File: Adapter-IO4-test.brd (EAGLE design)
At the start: 50 x 50 mm, 19 parts, among them CON1 RJ12/6, CON2 0.100, Q1 P-FET, Q2 P-FET, Q3 P-FET, Q4 P-FET, SW1 SPST-MOM, SW2 SPST-MOM, SW3 SPST-MOM, SW4 SPST-MOM

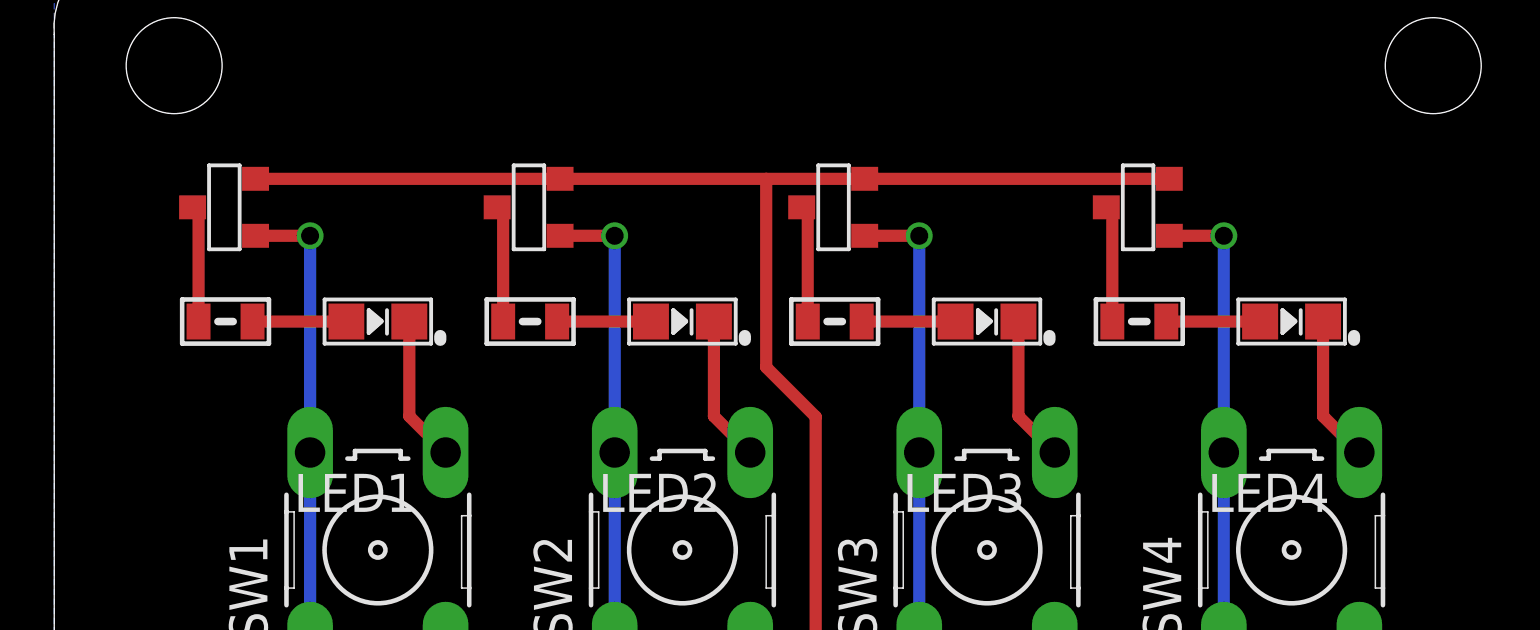
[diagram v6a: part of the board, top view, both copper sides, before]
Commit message: normalized values
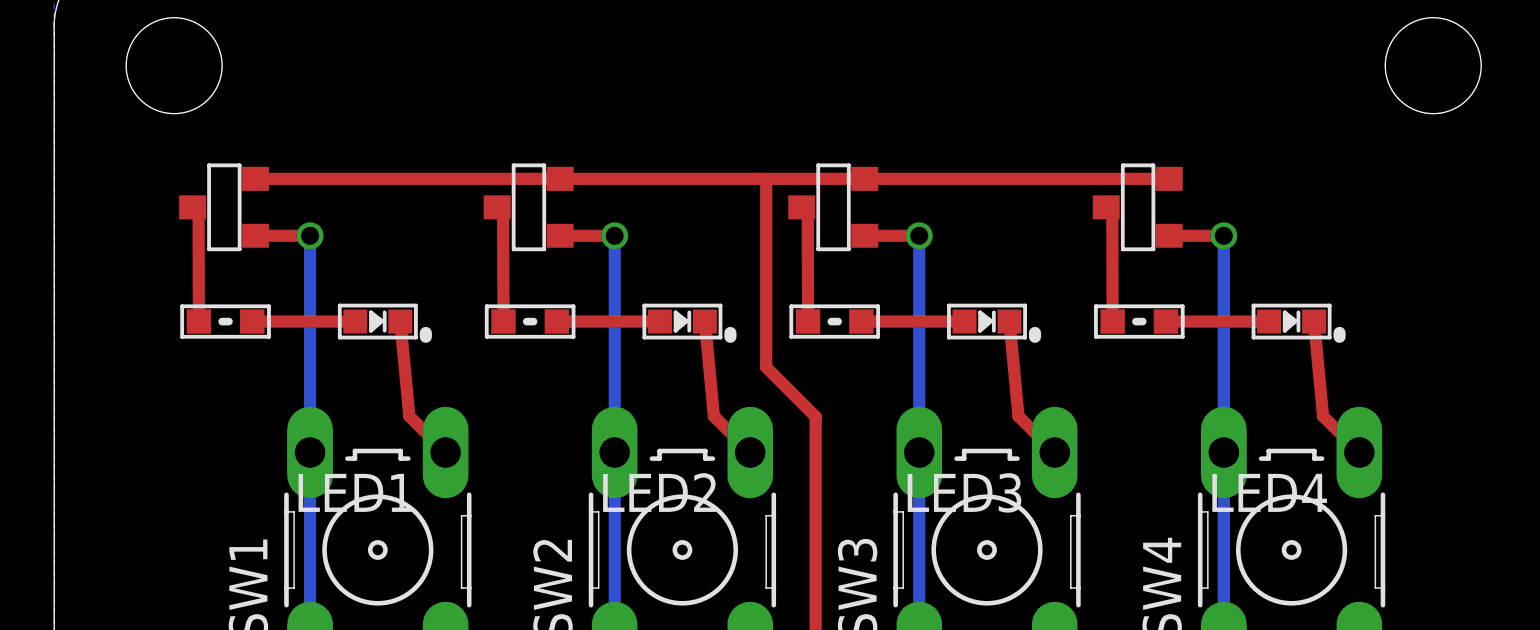
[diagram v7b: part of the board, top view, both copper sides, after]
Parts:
- LED1, LED2, LED3, LED4: device SPCoast:0805-LED -> SPCoast:0603-LED
- R1, R2, R3, R4: device SPCoast:0805-RES -> SPCoast:0603-RES
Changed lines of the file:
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@@
 <attribute name="VALUE" x="46.355" y="26.797" size="1.27" layer="27" ratio="10" rot="R90"/>
 </element>
-<element name="LED1" library="SPCoast" package="0805-LED" value="G" x="10.795" y="37.465" smashed="yes" rot="R180">
+<element name="LED1" library="SPCoast" package="0603-LED" value="G" x="10.795" y="37.465" smashed="yes" rot="R180">
 <attribute name="NAME" x="12.065" y="32.385" size="1.27" layer="25" rot="R180"/>
 <attribute name="VALUE" x="12.065" y="40.005" size="1.27" layer="27" rot="R180"/>
 </element>
-<element name="LED2" library="SPCoast" package="0805-LED" value="G" x="20.955" y="37.465" smashed="yes" rot="R180">
+<element name="LED2" library="SPCoast" package="0603-LED" value="G" x="20.955" y="37.465" smashed="yes" rot="R180">
 <attribute name="NAME" x="22.225" y="32.385" size="1.27" layer="25" rot="R180"/>
 <attribute name="VALUE" x="22.225" y="40.005" size="1.27" layer="27" rot="R180"/>
 </element>
-<element name="LED3" library="SPCoast" package="0805-LED" value="G" x="31.115" y="37.465" smashed="yes" rot="R180">
+<element name="LED3" library="SPCoast" package="0603-LED" value="G" x="31.115" y="37.465" smashed="yes" rot="R180">
 <attribute name="NAME" x="32.385" y="32.385" size="1.27" layer="25" rot="R180"/>
 <attribute name="VALUE" x="32.385" y="40.005" size="1.27" layer="27" rot="R180"/>
 </element>
-<element name="LED4" library="SPCoast" package="0805-LED" value="G" x="41.275" y="37.465" smashed="yes" rot="R180">
+<element name="LED4" library="SPCoast" package="0603-LED" value="G" x="41.275" y="37.465" smashed="yes" rot="R180">
 <attribute name="NAME" x="42.545" y="32.385" size="1.27" layer="25" rot="R180"/>
 <attribute name="VALUE" x="42.545" y="40.005" size="1.27" layer="27" rot="R180"/>
 </element>
-<element name="R1" library="SPCoast" package="0805-RES" value="2k0" x="5.715" y="37.465" smashed="yes" rot="R180">
+<element name="R1" library="SPCoast" package="0603-RES" value="2k0" x="5.715" y="37.465" smashed="yes" rot="R180">
 <attribute name="VALUE" x="6.731" y="38.862" size="0.4064" layer="27" rot="R180"/>
 </element>
-<element name="R2" library="SPCoast" package="0805-RES" value="2k0" x="15.875" y="37.465" smashed="yes" rot="R180">
+<element name="R2" library="SPCoast" package="0603-RES" value="2k0" x="15.875" y="37.465" smashed="yes" rot="R180">
 <attribute name="VALUE" x="16.891" y="38.862" size="0.4064" layer="27" rot="R180"/>
 </element>
-<element name="R3" library="SPCoast" package="0805-RES" value="2k0" x="26.035" y="37.465" smashed="yes" rot="R180">
+<element name="R3" library="SPCoast" package="0603-RES" value="2k0" x="26.035" y="37.465" smashed="yes" rot="R180">
 <attribute name="VALUE" x="27.051" y="38.862" size="0.4064" layer="27" rot="R180"/>
 </element>
-<element name="R4" library="SPCoast" package="0805-RES" value="2k0" x="36.195" y="37.465" smashed="yes" rot="R180">
+<element name="R4" library="SPCoast" package="0603-RES" value="2k0" x="36.195" y="37.465" smashed="yes" rot="R180">
 <attribute name="VALUE" x="37.211" y="38.862" size="0.4064" layer="27" rot="R180"/>
 </element>
@@
 <vertex x="50" y="50"/>
 </polygon>
-<wire x1="11.845" y1="37.465" x2="11.845" y2="34.3068" width="0.4064" layer="1"/>
+<wire x1="11.545" y1="37.465" x2="11.845" y2="34.3068" width="0.4064" layer="1"/>
 <wire x1="11.845" y1="34.3068" x2="13.0556" y2="33.0962" width="0.4064" layer="1"/>
-<wire x1="22.005" y1="37.465" x2="22.005" y2="34.3068" width="0.4064" layer="1"/>
+<wire x1="21.705" y1="37.465" x2="22.005" y2="34.3068" width="0.4064" layer="1"/>
 <wire x1="22.005" y1="34.3068" x2="23.2156" y2="33.0962" width="0.4064" layer="1"/>
-<wire x1="32.165" y1="37.465" x2="32.165" y2="34.3068" width="0.4064" layer="1"/>
+<wire x1="31.865" y1="37.465" x2="32.165" y2="34.3068" width="0.4064" layer="1"/>
 <wire x1="32.165" y1="34.3068" x2="33.3756" y2="33.0962" width="0.4064" layer="1"/>
-<wire x1="42.325" y1="37.465" x2="42.325" y2="34.3068" width="0.4064" layer="1"/>
+<wire x1="42.025" y1="37.465" x2="42.325" y2="34.3068" width="0.4064" layer="1"/>
 <wire x1="42.325" y1="34.3068" x2="43.5356" y2="33.0962" width="0.4064" layer="1"/>
 </signal>
@@
 <contactref element="Q1" pad="3"/>
 <contactref element="R1" pad="2"/>
-<wire x1="4.815" y1="37.465" x2="4.815" y2="41.075" width="0.4064" layer="1"/>
+<wire x1="4.826" y1="37.465" x2="4.815" y2="41.075" width="0.4064" layer="1"/>
 <wire x1="4.815" y1="41.075" x2="4.615" y2="41.275" width="0.4064" layer="1"/>
 </signal>
@@
 <contactref element="R1" pad="1"/>
 <contactref element="LED1" pad="A"/>
-<wire x1="6.615" y1="37.465" x2="9.745" y2="37.465" width="0.4064" layer="1"/>
+<wire x1="6.604" y1="37.465" x2="10.045" y2="37.465" width="0.4064" layer="1"/>
 </signal>
 <signal name="N$3">
 <contactref element="Q2" pad="3"/>
 <contactref element="R2" pad="2"/>
-<wire x1="14.975" y1="37.465" x2="14.975" y2="41.075" width="0.4064" layer="1"/>
+<wire x1="14.986" y1="37.465" x2="14.975" y2="41.075" width="0.4064" layer="1"/>
 <wire x1="14.975" y1="41.075" x2="14.775" y2="41.275" width="0.4064" layer="1"/>
 </signal>
@@
 <contactref element="R2" pad="1"/>
 <contactref element="LED2" pad="A"/>
-<wire x1="16.775" y1="37.465" x2="19.905" y2="37.465" width="0.4064" layer="1"/>
+<wire x1="16.764" y1="37.465" x2="20.205" y2="37.465" width="0.4064" layer="1"/>
 </signal>
 <signal name="N$5">
 <contactref element="Q3" pad="3"/>
 <contactref element="R3" pad="2"/>
-<wire x1="25.135" y1="37.465" x2="25.135" y2="41.075" width="0.4064" layer="1"/>
+<wire x1="25.146" y1="37.465" x2="25.135" y2="41.075" width="0.4064" layer="1"/>
 <wire x1="25.135" y1="41.075" x2="24.935" y2="41.275" width="0.4064" layer="1"/>
 </signal>
@@
 <contactref element="R3" pad="1"/>
 <contactref element="LED3" pad="A"/>
-<wire x1="26.935" y1="37.465" x2="30.065" y2="37.465" width="0.4064" layer="1"/>
+<wire x1="26.924" y1="37.465" x2="30.365" y2="37.465" width="0.4064" layer="1"/>
 </signal>
 <signal name="N$15">
 <contactref element="Q4" pad="3"/>
 <contactref element="R4" pad="2"/>
-<wire x1="35.295" y1="37.465" x2="35.295" y2="41.075" width="0.4064" layer="1"/>
+<wire x1="35.306" y1="37.465" x2="35.295" y2="41.075" width="0.4064" layer="1"/>
 <wire x1="35.295" y1="41.075" x2="35.095" y2="41.275" width="0.4064" layer="1"/>
 </signal>
@@
 <contactref element="R4" pad="1"/>
 <contactref element="LED4" pad="A"/>
-<wire x1="37.095" y1="37.465" x2="40.225" y2="37.465" width="0.4064" layer="1"/>
+<wire x1="37.084" y1="37.465" x2="40.525" y2="37.465" width="0.4064" layer="1"/>
 </signal>
 </signals>
